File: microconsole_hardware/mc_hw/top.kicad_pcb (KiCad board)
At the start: 2 copper layers, 161 x 96 mm, 110 parts, among them J1 USB_C_Receptacle_USB2.0_16P, Q1 Q_PMOS_GSD, SW10 TL3301NF160QG, SW11 TL3301NF160QG, SW12 TL3301NF160QG, SW13 TL3301NF160QG, SW14 TL3301NF160QG, SW15 TL3301NF160QG, SW16 Joystick, SW17 Joystick, SW19 SPDT_Slide_PTH_11.6x4.0mm, SW2 TL3301NF160QG, SW3 TL3301NF160QG, SW4 TL3301NF160QG, SW5 TL3301NF160QG, SW6 TL3301NF160QG, SW7 TL3301NF160QG, SW8 TL3301NF160QG, SW9 TL3301NF160QG, U1 MCP73833-FCI/UN, U2 S2B-PH-K-S, U3 MCP23017-E/SO, U4 ADS7828E/2K5, U5 PCM5102APWR, U6 PAM8302AADCR, U7 PAM8406DR

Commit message: fix up power and parts
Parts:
- added Q2: DMP2035U-7, Package_TO_SOT_SMD:SOT-23, F.Cu at (142.1, 66.9)
- added R31: 100k, PCM_SparkFun-Resistor:R_0603_1608Metric, F.Cu at (138.0, 67.0)
- Q1: value Q_PMOS_GSD -> DMP2035U-7
- turned D1 to 90 degrees
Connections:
- C2 pad 1: Net-(C2-Pad1) -> BAT+
- D1 pad 1: USB-VBUS -> SYS_RAW
- D1 pad 2: SYS_RAW -> USB-VBUS
- Q1 pad 2: BAT+ -> SYS_RAW
- Q1 pad 3: SYS_RAW -> BAT+
- SW19 pad 1: VSYS_BAT -> GND
- SW19 pad 2: SYS_RAW -> PWR_SW_GATE
- U2 pad 2: Net-(C2-Pad1) -> GND
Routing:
- net GND: track 900.2 -> 916.9 mm, vias 13 -> 14
- net 3v3: track 337.5 -> 322.4 mm
- net PWR_SW_GATE: track 0.00 -> 11.4 mm
- net SYS_RAW: track 75.7 -> 64.5 mm, vias 1 -> 2
- net Net-(C2-Pad1): track 5.45 -> 0.00 mm
- net BAT+: track 28.2 -> 33.6 mm
- net USB-VBUS: track 79.4 -> 76.9 mm
- net VSYS_BAT: track 110.6 -> 111.9 mm, vias 2 -> 3

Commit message: eh more fixes
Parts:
- D1: value D_Schottky -> PMEG40T30ER Schottky
- R9: value 2k -> 3.32k
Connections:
- A2 pad 40: VSYS_BAT -> unconnected-(A2-VBUS-Pad40)
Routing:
- net VSYS_BAT: track 111.9 -> 108.5 mm
- net unconnected-(A2-AGND-Pad33): track 0.80 -> 0.00 mm
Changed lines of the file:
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@@
 		(sheetname "/Battery/")
 		(sheetfile "battery.kicad_sch")
+		(units
+			(unit
+				(name "A")
+				(pins "1" "3" "2")
+			)
+		)
 		(attr smd)
 		(duplicate_pad_numbers_are_jumpers no)
@@
 			(layers "*.Cu" "*.Mask")
 			(remove_unused_layers no)
-			(net "unconnected-(A2-AGND-Pad33)")
+			(net "unconnected-(A2-AGND-Pad33)_1")
 			(pinfunction "AGND_33")
-			(pintype "power_out")
+			(pintype "power_out+no_connect")
 			(options
 				(clearance outline)
@@
 			(net "unconnected-(A2-AGND-Pad33)")
 			(pinfunction "AGND_33")
-			(pintype "power_out")
+			(pintype "power_out+no_connect")
 			(options
 				(clearance outline)
@@
 			(layers "*.Cu" "*.Mask")
 			(remove_unused_layers no)
-			(net "VSYS_BAT")
+			(net "unconnected-(A2-VBUS-Pad40)_1")
 			(pinfunction "VBUS_40")
-			(pintype "power_out")
+			(pintype "power_out+no_connect")
 		)
 		(pad "40" smd roundrect
@@
 			(layers "B.Cu" "B.Mask")
 			(roundrect_rratio 0.5)
-			(net "VSYS_BAT")
+			(net "unconnected-(A2-VBUS-Pad40)")
 			(pinfunction "VBUS_40")
-			(pintype "power_out")
+			(pintype "power_out+no_connect")
 		)
 		(zone
@@
 			)
 		)
-		(property "Value" "D_Schottky"
+		(property "Value" "PMEG40T30ER Schottky"
 			(at 0 -2.000001 90)
 			(layer "B.Fab")
@@
 			)
 		)
-		(property "Value" "2k"
+		(property "Value" "3.32k"
 			(at 0 -1.43 90)
 			(layer "B.Fab")
@@
 	)
 	(segment
-		(start 105.22 70.98)
-		(end 104.42 70.98)
-		(width 0.2)
-		(layer "B.Cu")
-		(net "VSYS_BAT")
-	)
-	(segment
 		(start 131.91 73.41)
 		(end 130.7443 73.41)
@@
 	)
 	(segment
-		(start 105.22 70.98)
-		(end 105.22 73.52)
-		(width 0.2)
-		(layer "B.Cu")
-		(net "VSYS_BAT")
-	)
-	(segment
 		(start 90.5 82.1)
 		(end 89.8557 82.1)
@@
 	)
 	(segment
-		(start 105.22 88.76)
-		(end 104.42 88.76)
-		(width 0.2)
-		(layer "B.Cu")
-		(net "unconnected-(A2-AGND-Pad33)")
-	)
-	(segment

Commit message: fixup
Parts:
- added D5: BAT54C, Package_TO_SOT_SMD:SOT-23, F.Cu at (129.8, 66.1)
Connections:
- A2 pad 40: unconnected-(A2-VBUS-Pad40) -> PICO_VBUS
- Q1 pad 1: USB-VBUS -> Net-(Q1-G)
- R5 pad 1: USB-VBUS -> Net-(Q1-G)
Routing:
- net Net-(Q1-G): track 0.00 -> 92.3 mm, vias 0 -> 3
- net PICO_VBUS: track 0.00 -> 28.1 mm, vias 0 -> 1
- net USB-VBUS: track 76.9 -> 89.5 mm, vias 6 -> 9

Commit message: fix up
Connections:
- net MCP RESET renamed Net-(U3-~{RESET})

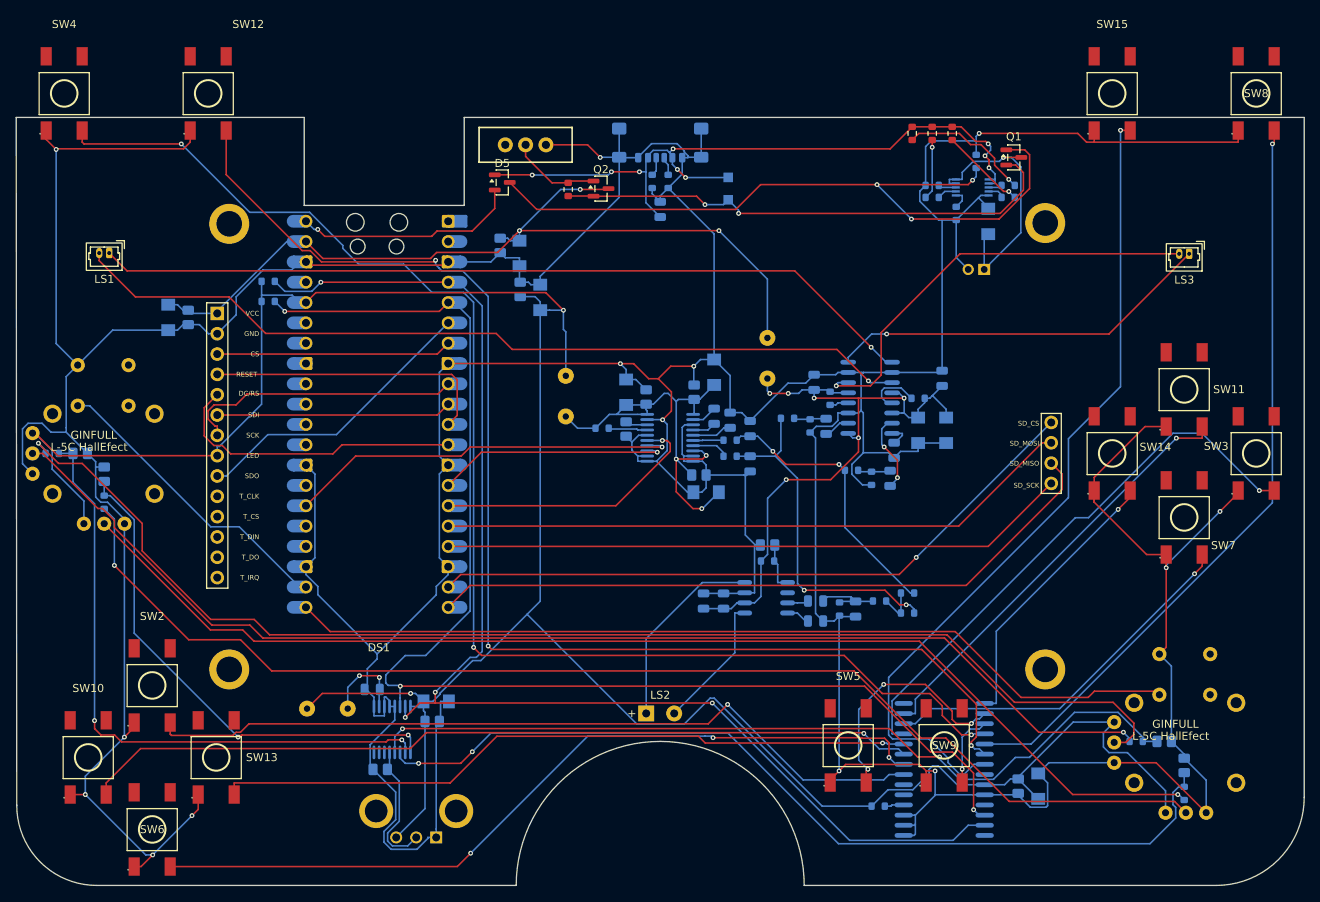
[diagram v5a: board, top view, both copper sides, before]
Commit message: fix audio gain, relocated shoulder buttons, round pcb edges
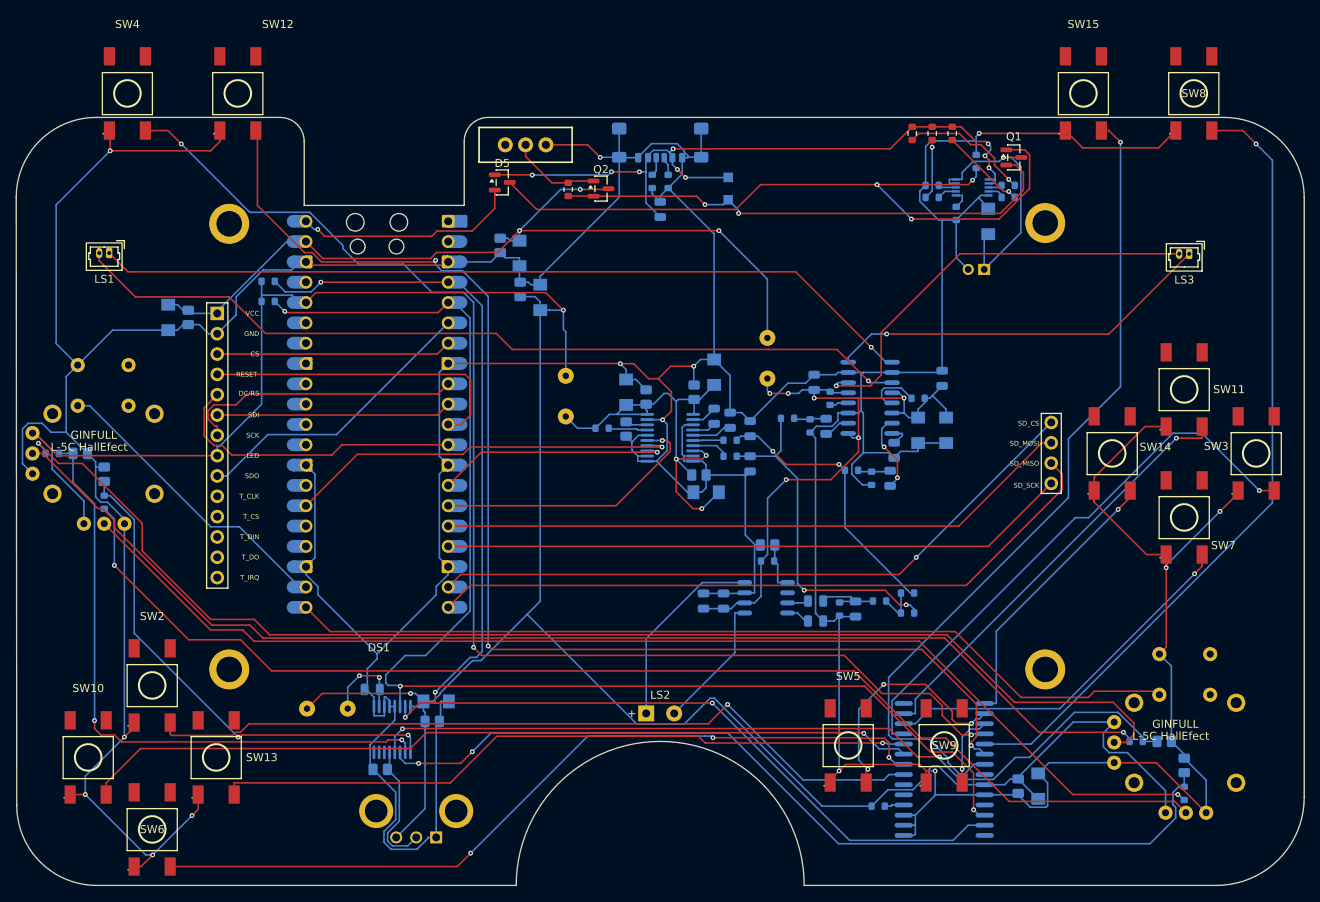
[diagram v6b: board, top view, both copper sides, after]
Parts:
- R22, R29: value 22k OHM -> 27k OHM 1%
- R23, R28: value 2.2k OHM -> 2k OHM 1%
- moved SW4 7.90 mm to (82.9, 55.0)
- moved SW8 7.80 mm to (216.2, 55.0)
- moved SW12 3.70 mm to (96.7, 55.0)
- moved SW15 3.60 mm to (202.4, 55.0)
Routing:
- net GND: track 916.9 -> 906.6 mm
- net MCP GPB3 / L1: track 171.2 -> 162.3 mm
- net MCP GPB4 / R1: track 95.1 -> 100.4 mm
- net GPIO8 / LCD RESET: track 37.1 -> 40.4 mm
- net MCP GPB5 / L2: track 160.3 -> 158.8 mm
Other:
- outline, holes or cut-outs redrawn

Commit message: fix ferrite beads.
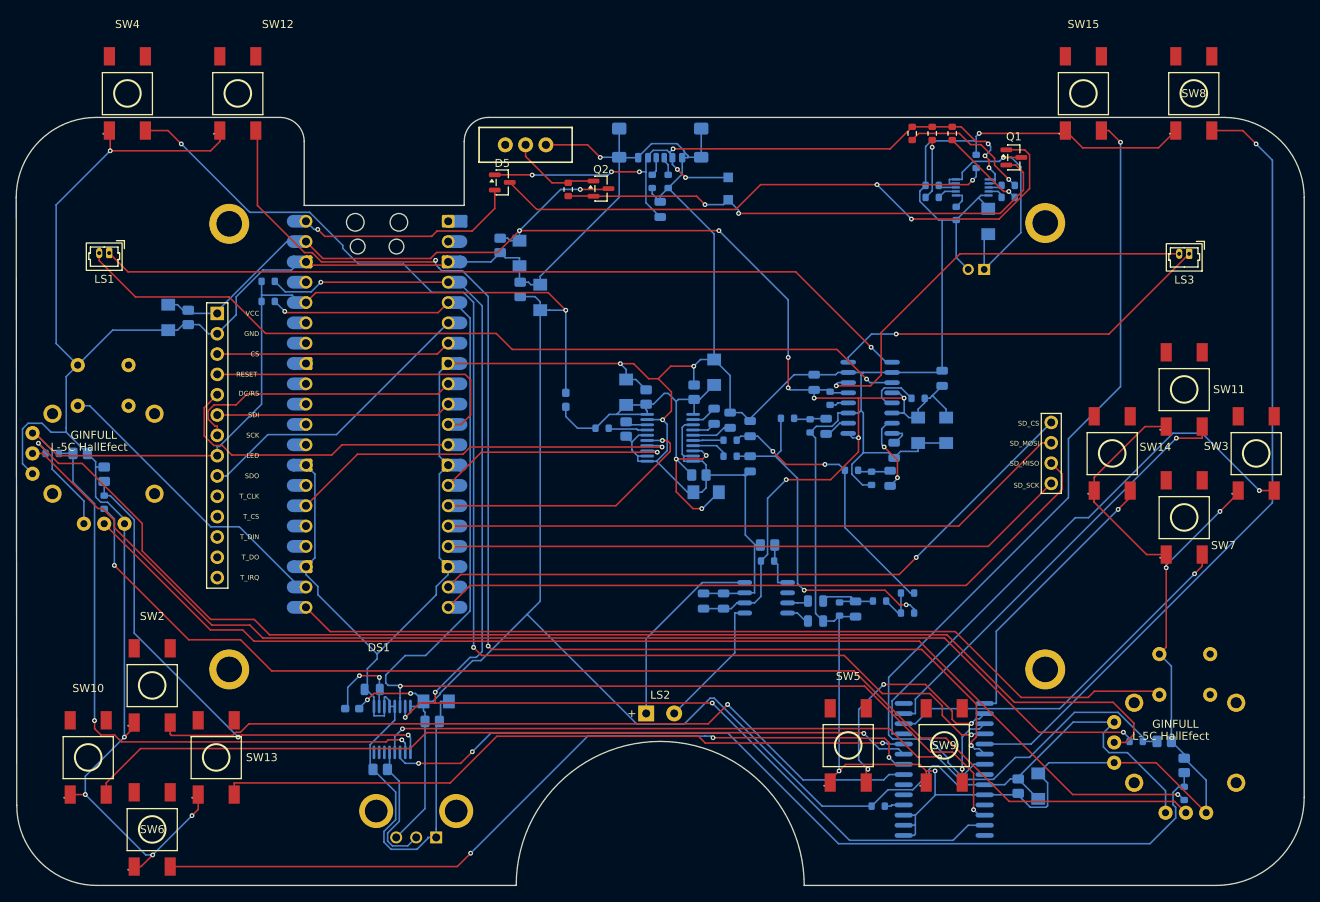
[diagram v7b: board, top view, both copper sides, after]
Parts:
- removed FB5: FerriteBead_Small, Ferrite_THT:LairdTech_28C0236-0JW-10
- FB1, FB4: value FerriteBead_Small -> MPZ1608S601ATA00 FerriteBead; footprint Ferrite_THT:LairdTech_28C0236-0JW-10 -> Inductor_SMD:L_0603_1608Metric_Pad1.05x0.95mm_HandSolder
- moved FB1 5.64 mm to (111.0, 131.9), turned to 180 degrees
- moved FB4 3.00 mm to (137.7, 93.3)
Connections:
- A2 pad 39: VSYS_BAT -> AMP_VDD
- C45 pad 2: VSYS_BAT -> AMP_VDD
- C46 pad 1: VSYS_BAT -> AMP_VDD
- C47 pad 2: VSYS_BAT -> AMP_VDD
- C48 pad 2: VSYS_BAT -> AMP_VDD
- DS1 pad 1: VSYS_BAT -> AMP_VDD
- Q2 pad 3: VSYS_BAT -> AMP_VDD
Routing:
- net AMP_VDD: track 83.0 -> 194.5 mm, vias 6 -> 9
- net VSYS_BAT: track 108.5 -> 0.00 mm, vias 3 -> 0
- net 3v3: track 322.4 -> 318.5 mm, vias 2 -> 3
- net 3v3_AUDIO: track 56.3 -> 57.5 mm
